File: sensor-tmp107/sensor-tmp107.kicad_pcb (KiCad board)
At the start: 2 copper layers, 35.6 x 32 mm, 12 parts, among them J1 DE9_Socket_MountingHoles, J2 DE9_Socket_MountingHoles, Q1 SS8050, Q2 SS8050, U1 TMP107BIDR

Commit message: Duuuze pady
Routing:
- net Net-(U1-ALERT2): track 9.42 -> 8.23 mm
- net Net-(U1-R1): track 75.6 -> 74.9 mm

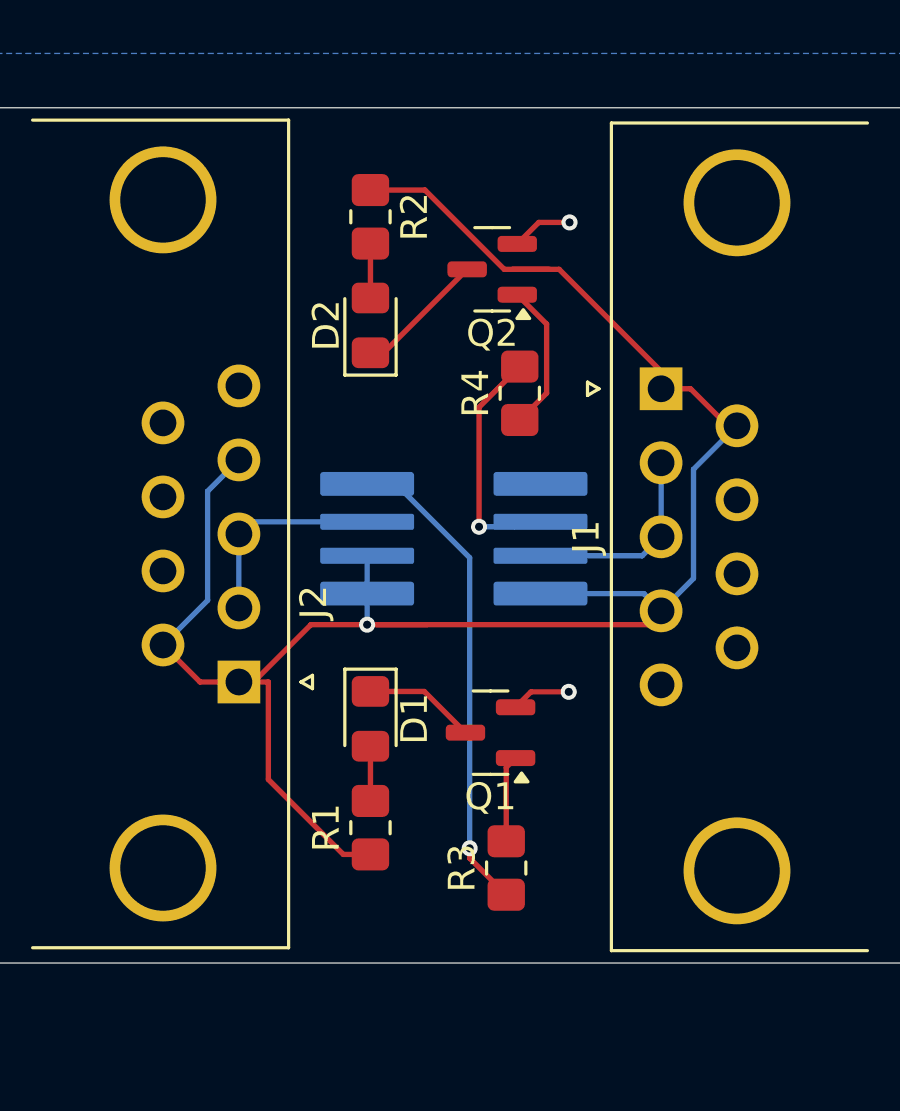
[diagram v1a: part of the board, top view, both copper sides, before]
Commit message: Added capcaitors, text improvements
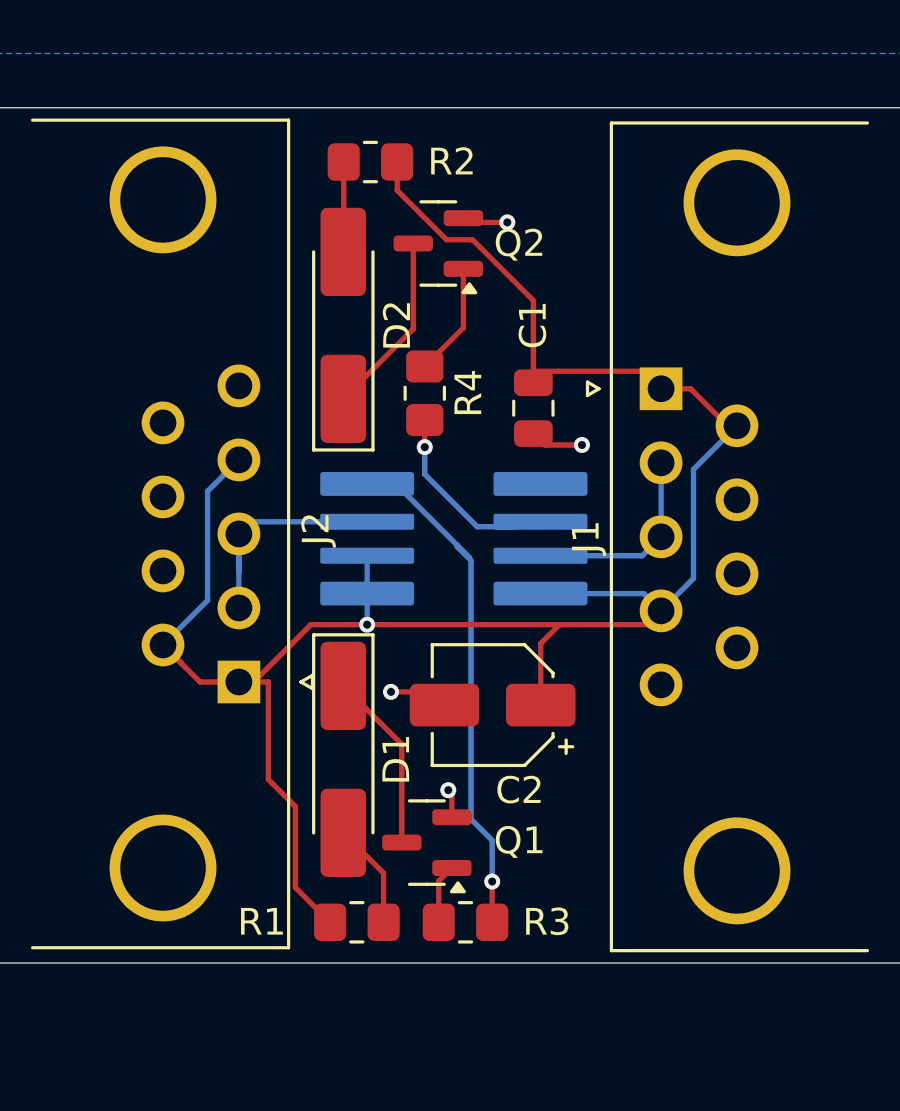
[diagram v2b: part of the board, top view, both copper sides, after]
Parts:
- added C1: 100nF, Capacitor_SMD:C_0805_2012Metric, F.Cu at (138.7, 82.4)
- added C2: 10uF, Capacitor_SMD:CP_Elec_4x5.4, F.Cu at (137.2, 93.5)
- D1, D2: footprint LED_SMD:LED_0805_2012Metric_Pad1.15x1.40mm_HandSolder -> Diode_SMD:D_MiniMELF_Handsoldering
- moved Q1 4.75 mm to (134.7, 98.6)
- moved G*** 3.66 mm to (136.1, 87.4), turned to -90 degrees
- moved R1 3.58 mm to (132.1, 101.6), turned to 0 degrees
- moved R4 3.56 mm to (134.6, 81.8), turned to -90 degrees
- moved R3 2.54 mm to (136.1, 101.6), turned to 180 degrees
- moved Q2 2.24 mm to (135.1, 76.2)
- moved R2 2.05 mm to (132.6, 73.2), turned to 180 degrees
- moved D1 1.83 mm to (131.6, 95.5)
- moved D2 1.02 mm to (131.6, 79.3)
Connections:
- net Net-(U1-R1) renamed /5V
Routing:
- net /5V: track 74.9 -> 77.7 mm
- net Net-(D1-K): track 4.19 -> 6.77 mm
- net Net-(U1-ALERT2): track 8.23 -> 6.22 mm
- net Net-(D2-K): track 4.91 -> 6.90 mm
- net Net-(D1-A): track 2.05 -> 3.97 mm
- net GND: track 4.52 -> 6.06 mm, vias 2 -> 4
- net Net-(D2-A): track 2.04 -> 3.35 mm
- net Net-(Q2-B): track 5.56 -> 4.25 mm
- net Net-(U1-ALERT1): track 17.3 -> 18.3 mm
- net Net-(Q1-B): track 3.26 -> 2.24 mm
- net Net-(U1-I/O2): track 8.35 -> 7.58 mm

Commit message: Update sensor pcb
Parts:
- D1, D2: footprint Diode_SMD:D_MiniMELF_Handsoldering -> LED_SMD:LED_0805_2012Metric
- R1, R2, R3, R4: footprint Resistor_SMD:R_0805_2012Metric_Pad1.20x1.40mm_HandSolder -> Resistor_SMD:R_0805_2012Metric
- moved R2 5.59 mm to (132.6, 78.7), turned to -90 degrees
- moved R3 3.66 mm to (138.2, 98.6), turned to -90 degrees
- moved D2 3.27 mm to (132.6, 82.4)
- moved D1 2.74 mm to (132.6, 93.0), turned to 90 degrees
- moved Q2 2.59 mm to (135.6, 78.7)
- moved R4 1.64 mm to (136.1, 82.4)
- moved R1 0.72 mm to (132.6, 101.1), turned to 90 degrees
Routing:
- net Net-(D1-A): track 3.97 -> 9.03 mm
- net Net-(U1-ALERT1): track 18.3 -> 14.8 mm
- net /5V: track 77.7 -> 74.6 mm
- net Net-(U1-I/O1): track 8.50 -> 6.21 mm
- net Net-(Q2-B): track 4.25 -> 1.97 mm
- net Net-(D1-K): track 6.77 -> 5.20 mm
- net Net-(D2-A): track 3.35 -> 1.78 mm
- net Net-(D2-K): track 6.90 -> 5.45 mm
- net Net-(U1-ALERT2): track 6.22 -> 5.08 mm

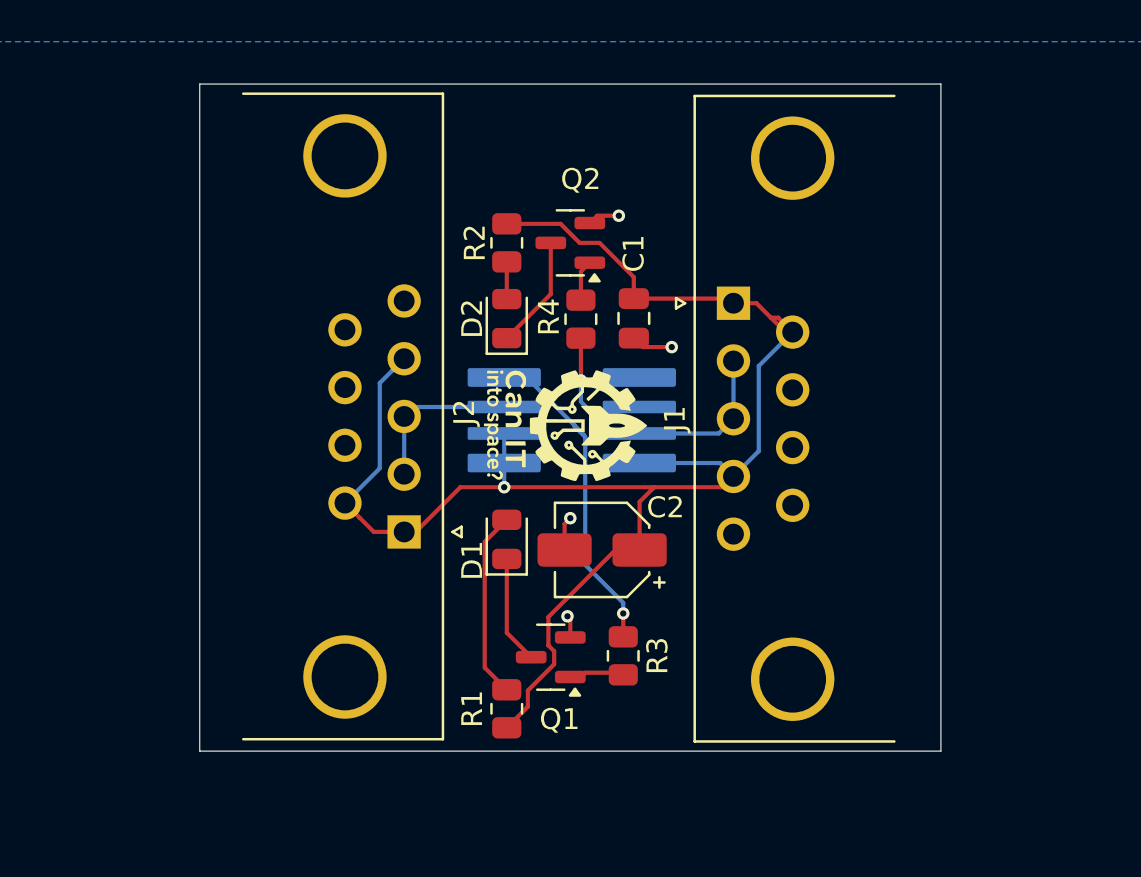
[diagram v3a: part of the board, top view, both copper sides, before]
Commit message: Fix rs232 port footprint
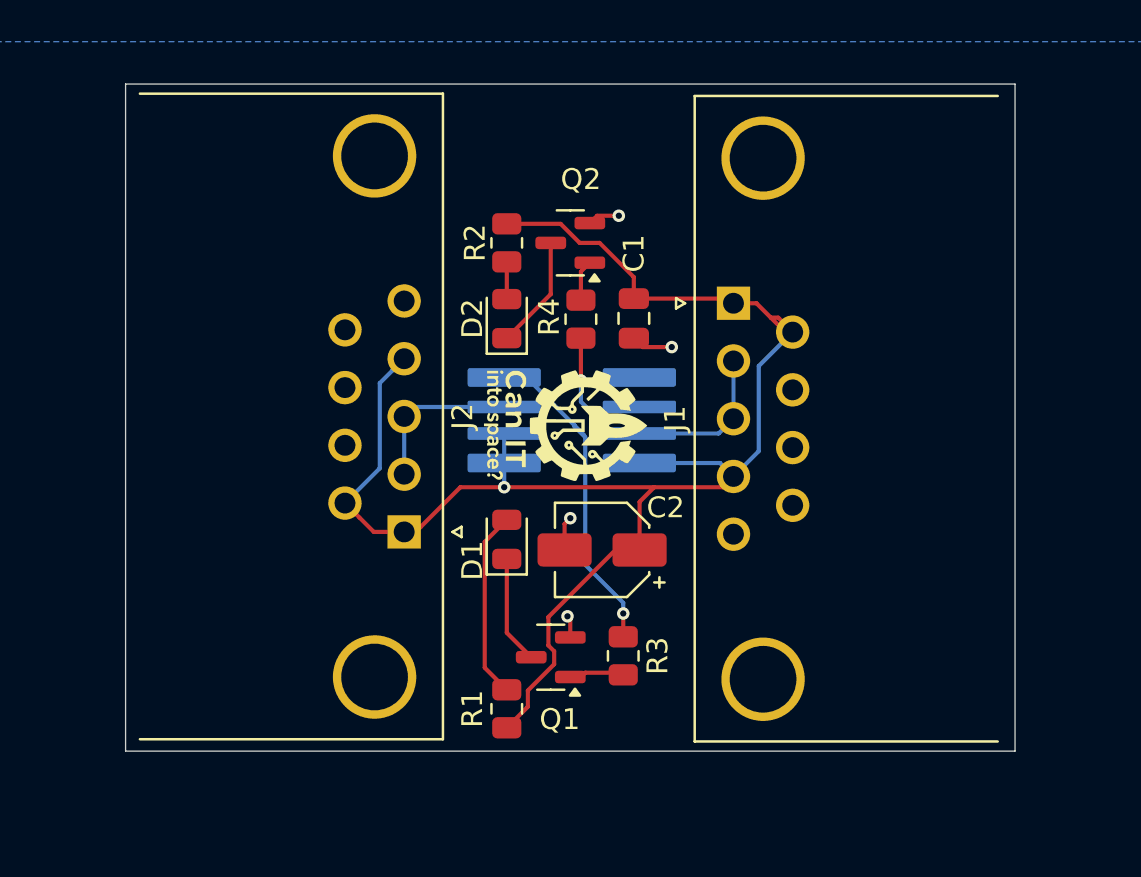
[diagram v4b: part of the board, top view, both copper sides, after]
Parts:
- J1, J2: footprint Connector_Dsub:DSUB-9_Socket_Horizontal_P2.77x2.84mm_EdgePinOffset4.94mm_Housed_MountingHolesOffset4.94mm -> Connector_Dsub:DSUB-9_Socket_Horizontal_P2.77x2.84mm_EdgePinOffset9.90mm_Housed_MountingHolesOffset11.32mm
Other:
- board size 35.6 x 32 mm -> 42.7 x 32 mm

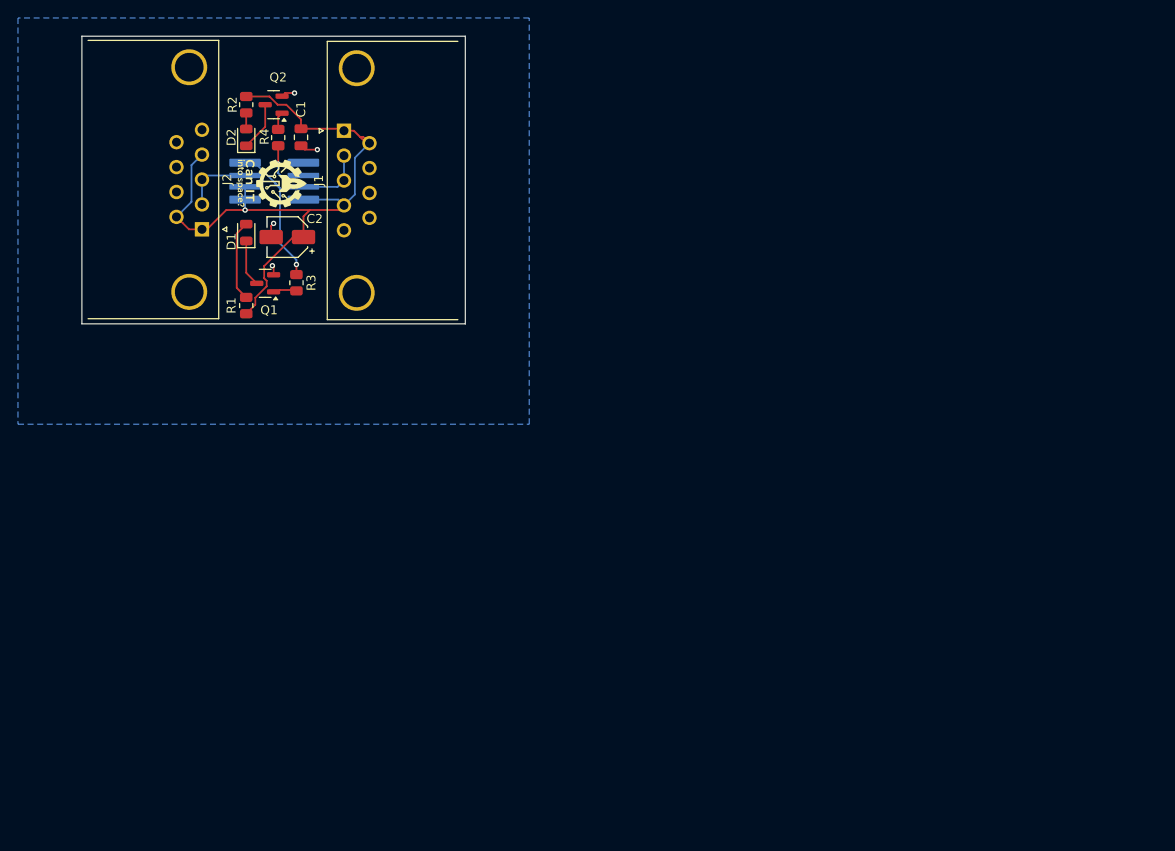
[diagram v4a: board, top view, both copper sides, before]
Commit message: Rework pcb to make it easier to attach mechanically
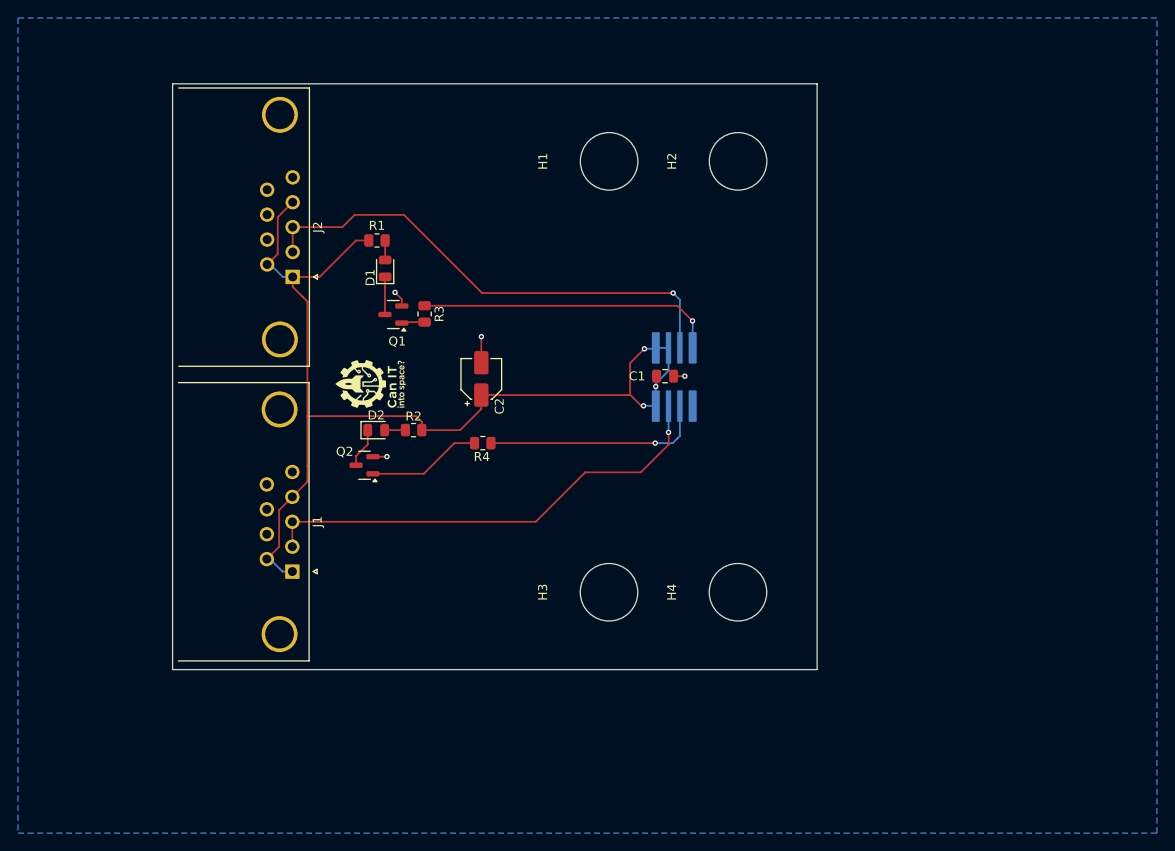
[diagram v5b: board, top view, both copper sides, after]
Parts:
- added H1: MountingHole_Pad_MP, MountingHole:MountingHole_6.4mm_M6, F.Cu at (173.0, 85.0)
- added H2: MountingHole_Pad_MP, MountingHole:MountingHole_6.4mm_M6, F.Cu at (187.3, 85.0)
- added H3: MountingHole_Pad_MP, MountingHole:MountingHole_6.4mm_M6, F.Cu at (173.0, 133.0)
- added H4: MountingHole_Pad_MP, MountingHole:MountingHole_6.4mm_M6, F.Cu at (187.3, 133.0)
- D1: value LED -> LED żółtozielony
- D2: value LED -> LED czerwony
- Q1, Q2: value SS8050 -> MMBT3904
- R1, R2: value 160 -> 200
- moved U1 49.6 mm to (180.2, 109.0), turned to -90 degrees
- moved J1 49.4 mm to (137.7, 130.7), turned to -90 degrees
- moved C1 48.5 mm to (179.2, 109.0), turned to 0 degrees
- moved Q2 41.4 mm to (145.8, 118.9)
- moved R4 40.9 mm to (158.9, 116.4), turned to 0 degrees
- moved R2 40.7 mm to (151.2, 115.0), turned to 180 degrees
- moved D2 35.6 mm to (147.1, 115.0), turned to 0 degrees
- moved C2 26.7 mm to (158.8, 109.2), turned to 90 degrees
- moved G*** 24.5 mm to (145.7, 110.0), turned to 90 degrees
- moved R1 16.3 mm to (147.1, 93.8), turned to 0 degrees
- moved D1 16.0 mm to (148.1, 97.0)
- moved Q1 14.7 mm to (149.0, 102.1)
- moved R3 14.7 mm to (152.4, 102.0)
- moved J2 11.4 mm to (137.8, 97.9)
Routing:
- net Net-(U1-I/O1): track 6.21 -> 55.7 mm, vias 0 -> 1
- net Net-(U1-I/O2): track 7.58 -> 52.5 mm, vias 0 -> 1
- net /5V: track 74.6 -> 118.8 mm, vias 1 -> 3
- net Net-(U1-ALERT2): track 5.08 -> 24.7 mm
- net Net-(U1-ALERT1): track 14.8 -> 33.5 mm
- net Net-(Q2-B): track 1.97 -> 12.7 mm
- net Net-(D1-A): track 9.03 -> 2.18 mm
- net GND: track 6.24 -> 7.55 mm
- net Net-(D1-K): track 5.20 -> 4.20 mm
- net Net-(D2-K): track 5.45 -> 4.45 mm
- net Net-(D2-A): track 1.78 -> 2.31 mm
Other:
- board size 42.7 x 32 mm -> 71.7 x 65.2 mm
